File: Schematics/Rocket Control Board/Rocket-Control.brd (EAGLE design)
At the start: 21.9 x 35.5 mm, 23 parts

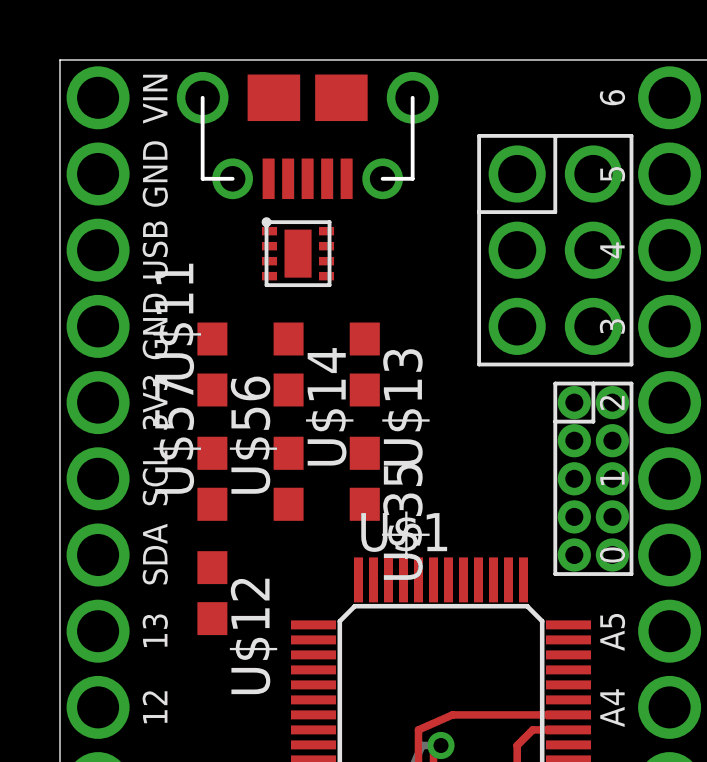
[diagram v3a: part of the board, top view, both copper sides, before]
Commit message: Added Diode, Began Routing
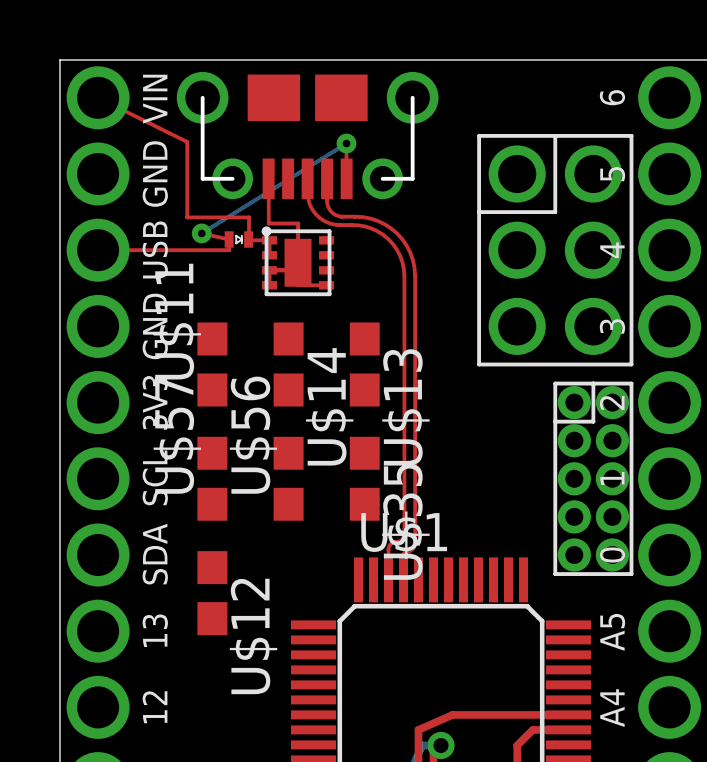
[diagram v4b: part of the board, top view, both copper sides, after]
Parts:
- added U$15: REGULATION-DIODE, RocketControlBoard:SOD-882
- moved U$5 0.30 mm to (6.99, 29.5)
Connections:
- net USB: now also U$15.P$1
- net VIN: now also U$15.P$2
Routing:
- net USB-P: track 0.00 -> 15.2 mm
- net USB-N: track 0.00 -> 15.0 mm
- net USB: track 0.00 -> 12.5 mm, vias 0 -> 2
- net VIN: track 0.00 -> 9.84 mm
- net GND: track 28.7 -> 37.2 mm
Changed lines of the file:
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@@
 <?xml version="1.0" encoding="utf-8"?>
 <!DOCTYPE eagle SYSTEM "eagle.dtd">
-<eagle version="7.5.0">
+<eagle version="7.6.0">
 <drawing>
 <settings>
@@
 <element name="U$21" library="RocketControlBoard" package="HEADER-SIDE-A" value="HEADER-SIDE-A" x="20.32" y="16.51"/>
 <element name="U$22" library="RocketControlBoard" package="HEADER-SIDE-B" value="HEADER-SIDE-B" x="1.27" y="36.83" rot="R90"/>
-<element name="U$5" library="RocketControlBoard" package="8-WFDFN-EXPOSED-PAD" value="REGULATOR" x="6.985" y="29.845" rot="R270"/>
+<element name="U$5" library="RocketControlBoard" package="8-WFDFN-EXPOSED-PAD" value="REGULATOR" x="6.985" y="29.5402" rot="R270"/>
 <element name="U$11" library="RocketControlBoard" package="C0603" value="REGULATOR-CAPACITORS" x="5.08" y="25.4" rot="R90"/>
 <element name="U$12" library="RocketControlBoard" package="C0603" value="REGULATOR-CAPACITORS" x="5.08" y="17.78" rot="R270"/>
 <element name="U$13" library="RocketControlBoard" package="C0603" value="REGULATOR-INDUCTOR" x="10.16" y="25.4" rot="R270"/>
 <element name="U$14" library="RocketControlBoard" package="C0603" value="REGULATOR-RESISTOR" x="7.62" y="25.4" rot="R270"/>
+<element name="U$15" library="RocketControlBoard" package="SOD-882" value="REGULATION-DIODE" x="5.6388" y="29.5656"/>
 </elements>
 <signals>
@@
 <contactref element="U$12" pad="1"/>
 <contactref element="U$5" pad="EXPOSED-THERMAL-PAD"/>
-<wire x1="8.885" y1="28.345" x2="7.935" y2="29.095" width="0" layer="19" extent="1-1"/>
-<wire x1="17.145" y1="19.05" x2="8.885" y2="28.345" width="0" layer="19" extent="1-1"/>
-<wire x1="10.16" y1="22.44" x2="17.145" y2="19.05" width="0" layer="19" extent="1-1"/>
-<wire x1="17.145" y1="21.59" x2="17.145" y2="19.05" width="0" layer="19" extent="1-1"/>
-<wire x1="17.145" y1="22.86" x2="17.145" y2="21.59" width="0" layer="19" extent="1-1"/>
-<wire x1="7.62" y1="22.44" x2="17.145" y2="21.59" width="0" layer="19" extent="1-1"/>
+<wire x1="6.985" y1="28.5402" x2="6.985" y2="28.0402" width="0.127" layer="1"/>
+<wire x1="8.885" y1="28.0402" x2="7.935" y2="28.0402" width="0.127" layer="1"/>
+<wire x1="7.935" y1="28.0402" x2="7.935" y2="28.7902" width="0.127" layer="1"/>
+<wire x1="6.985" y1="28.5402" x2="7.935" y2="28.5402" width="0.127" layer="1"/>
+<wire x1="7.935" y1="28.5402" x2="7.935" y2="28.7902" width="0.127" layer="1"/>
+<wire x1="6.955" y1="31.59" x2="6.9596" y2="31.59" width="0.127" layer="1"/>
+<wire x1="6.9596" y1="31.59" x2="6.9596" y2="30.099" width="0.127" layer="1"/>
+<wire x1="6.985" y1="28.5402" x2="7.9756" y2="28.5402" width="0.127" layer="1"/>
+<wire x1="7.9756" y1="28.5402" x2="7.9756" y2="28.829" width="0.127" layer="1"/>
+<wire x1="6.9596" y1="30.099" x2="7.935" y2="30.099" width="0.127" layer="1"/>
+<wire x1="7.935" y1="30.099" x2="7.935" y2="28.7902" width="0.127" layer="1"/>
+<wire x1="17.145" y1="22.86" x2="17.78" y2="26.67" width="0" layer="19" extent="1-1"/>
+<wire x1="17.145" y1="21.59" x2="17.145" y2="22.86" width="0" layer="19" extent="1-1"/>
+<wire x1="17.145" y1="19.05" x2="17.145" y2="21.59" width="0" layer="19" extent="1-1"/>
+<wire x1="16.95" y1="13.72" x2="17.145" y2="19.05" width="0" layer="19" extent="1-1"/>
+<wire x1="8.45" y1="14.22" x2="11.95" y2="13.22" width="0" layer="19" extent="1-1"/>
+<wire x1="10.45" y1="18.22" x2="8.45" y2="14.22" width="0" layer="19" extent="1-1"/>
+<wire x1="10.16" y1="22.44" x2="10.45" y2="18.22" width="0" layer="19" extent="1-1"/>
+<wire x1="7.62" y1="22.44" x2="10.16" y2="22.44" width="0" layer="19" extent="1-1"/>
 <wire x1="5.08" y1="22.44" x2="7.62" y2="22.44" width="0" layer="19" extent="1-1"/>
-<wire x1="10.45" y1="18.22" x2="5.08" y2="22.44" width="0" layer="19" extent="1-1"/>
-<wire x1="8.45" y1="14.22" x2="10.45" y2="18.22" width="0" layer="19" extent="1-1"/>
-<wire x1="11.95" y1="13.22" x2="8.45" y2="14.22" width="0" layer="19" extent="1-1"/>
-<wire x1="6.955" y1="31.59" x2="6.985" y2="28.845" width="0" layer="19" extent="1-1"/>
-<wire x1="17.78" y1="26.67" x2="6.955" y2="31.59" width="0" layer="19" extent="1-1"/>
-<wire x1="1.27" y1="26.67" x2="17.78" y2="26.67" width="0" layer="19" extent="1-1"/>
+<wire x1="5.08" y1="24.55" x2="5.08" y2="22.44" width="0" layer="19" extent="1-1"/>
+<wire x1="5.08" y1="18.63" x2="5.08" y2="22.44" width="0" layer="19" extent="1-1"/>
+<wire x1="6.985" y1="28.0402" x2="5.08" y2="24.55" width="0" layer="19" extent="1-1"/>
+<wire x1="1.27" y1="26.67" x2="5.08" y2="24.55" width="0" layer="19" extent="1-1"/>
 <wire x1="1.27" y1="31.75" x2="1.27" y2="26.67" width="0" layer="19" extent="1-1"/>
-<wire x1="5.08" y1="24.55" x2="8.89" y2="3.39" width="0" layer="19" extent="1-1"/>
-<wire x1="5.08" y1="18.63" x2="5.08" y2="24.55" width="0" layer="19" extent="1-1"/>
-<wire x1="7.935" y1="29.095" x2="6.985" y2="28.845" width="0" layer="19" extent="1-1"/>
-<wire x1="6.985" y1="28.845" x2="6.985" y2="28.345" width="0" layer="19" extent="1-1"/>
 </signal>
 <signal name="A0">
@@
 <contactref element="U$1" pad="33"/>
 <contactref element="U$38" pad="2:D-"/>
-<wire x1="11.45" y1="18.22" x2="8.905" y2="31.59" width="0" layer="19" extent="1-1"/>
+<wire x1="8.905" y1="31.59" x2="8.905" y2="30.8714" width="0.127" layer="1"/>
+<wire x1="8.905" y1="30.8714" x2="9.398" y2="30.3276" width="0.127" layer="1" curve="90"/>
+<wire x1="9.398" y1="30.3276" x2="9.8298" y2="30.3276" width="0.127" layer="1"/>
+<wire x1="9.8298" y1="30.3276" x2="11.8364" y2="28.3718" width="0.127" layer="1" curve="-90"/>
+<wire x1="11.8364" y1="28.3718" x2="11.8364" y2="19.4564" width="0.127" layer="1"/>
+<wire x1="11.8364" y1="19.4564" x2="11.5316" y2="19.1516" width="0.127" layer="1" curve="-90"/>
+<wire x1="11.5316" y1="19.1516" x2="11.45" y2="19.0192" width="0.127" layer="1" curve="90"/>
+<wire x1="11.45" y1="19.0192" x2="11.45" y2="18.22" width="0.127" layer="1"/>
 </signal>
 <signal name="USB-P">
 <contactref element="U$1" pad="34"/>
 <contactref element="U$38" pad="3:D+"/>
-<wire x1="10.95" y1="18.22" x2="8.255" y2="31.59" width="0" layer="19" extent="1-1"/>
+<wire x1="8.255" y1="31.59" x2="8.255" y2="31.1658" width="0.127" layer="1"/>
+<wire x1="8.255" y1="31.1658" x2="9.2964" y2="30.0482" width="0.127" layer="1" curve="90"/>
+<wire x1="9.2964" y1="30.0482" x2="9.7282" y2="30.0482" width="0.127" layer="1"/>
+<wire x1="9.7282" y1="30.0482" x2="11.4808" y2="28.3718" width="0.127" layer="1" curve="-90"/>
+<wire x1="11.4808" y1="28.3718" x2="11.4808" y2="19.7612" width="0.127" layer="1"/>
+<wire x1="11.4808" y1="19.7612" x2="11.2014" y2="19.4818" width="0.127" layer="1" curve="-90"/>
+<wire x1="11.2014" y1="19.4818" x2="10.95" y2="19.2304" width="0.127" layer="1" curve="90"/>
+<wire x1="10.95" y1="19.2304" x2="10.95" y2="18.22" width="0.127" layer="1"/>
 </signal>
 <signal name="VDDIO-B">
@@
 <contactref element="U$38" pad="1:VBUS"/>
 <contactref element="U$22" pad="USB"/>
-<wire x1="1.27" y1="29.21" x2="9.555" y2="31.59" width="0" layer="19" extent="1-1"/>
+<contactref element="U$15" pad="P$1"/>
+<wire x1="5.6388" y1="29.5656" x2="5.6388" y2="29.21" width="0.127" layer="1"/>
+<wire x1="5.6388" y1="29.21" x2="1.27" y2="29.21" width="0.127" layer="1"/>
+<wire x1="9.555" y1="31.59" x2="9.5504" y2="31.59" width="0.127" layer="1"/>
+<wire x1="9.5504" y1="31.59" x2="9.5504" y2="32.766" width="0.127" layer="1"/>
+<via x="9.5504" y="32.766" extent="1-16" drill="0.254"/>
+<wire x1="9.5504" y1="32.766" x2="4.7244" y2="29.7688" width="0.127" layer="16"/>
+<via x="4.7244" y="29.7688" extent="1-16" drill="0.254"/>
+<wire x1="4.7244" y1="29.7688" x2="5.6388" y2="29.5656" width="0.127" layer="1"/>
 </signal>
 <signal name="RX">
@@
 <contactref element="U$11" pad="2"/>
 <contactref element="U$5" pad="VIN"/>
-<wire x1="1.27" y1="34.29" x2="6.985" y2="29.845" width="0" layer="19" extent="1-1"/>
-<wire x1="5.08" y1="26.25" x2="6.985" y2="29.345" width="0" layer="19" extent="1-1"/>
-<wire x1="6.985" y1="29.345" x2="6.985" y2="29.845" width="0" layer="19" extent="1-1"/>
+<contactref element="U$15" pad="P$2"/>
+<wire x1="6.985" y1="29.5402" x2="6.3142" y2="29.5402" width="0.127" layer="1"/>
+<wire x1="6.3142" y1="29.5402" x2="6.2888" y2="29.5656" width="0.127" layer="1"/>
+<wire x1="5.08" y1="26.25" x2="6.985" y2="29.0402" width="0" layer="19" extent="1-1"/>
+<wire x1="6.985" y1="29.5402" x2="6.985" y2="29.0402" width="0.127" layer="1"/>
+<wire x1="6.2888" y1="29.5656" x2="6.2992" y2="29.5656" width="0.127" layer="1"/>
+<wire x1="6.2992" y1="29.5656" x2="6.2992" y2="30.3022" width="0.127" layer="1"/>
+<wire x1="6.2992" y1="30.3022" x2="4.2418" y2="30.3022" width="0.127" layer="1"/>
+<wire x1="4.2418" y1="30.3022" x2="4.2418" y2="32.8168" width="0.127" layer="1"/>
+<wire x1="4.2418" y1="32.8168" x2="1.27" y2="34.29" width="0.127" layer="1"/>
 </signal>
 <signal name="A5">
@@
 <contactref element="U$12" pad="2"/>
 <contactref element="U$5" pad="SW"/>
-<wire x1="5.08" y1="20.74" x2="8.885" y2="29.345" width="0" layer="19" extent="1-1"/>
+<wire x1="5.08" y1="20.74" x2="8.885" y2="29.0402" width="0" layer="19" extent="1-1"/>
 <wire x1="8.45" y1="13.22" x2="5.08" y2="20.74" width="0" layer="19" extent="1-1"/>
 <wire x1="5.08" y1="16.93" x2="8.45" y2="13.22" width="0" layer="19" extent="1-1"/>
@@
 <contactref element="U$5" pad="PG"/>
 <contactref element="U$13" pad="1"/>
-<wire x1="10.16" y1="26.25" x2="8.885" y2="29.845" width="0" layer="19" extent="1-1"/>
+<wire x1="10.16" y1="26.25" x2="8.885" y2="29.5402" width="0" layer="19" extent="1-1"/>
 </signal>
 <signal name="N$3">
 <contactref element="U$14" pad="1"/>
 <contactref element="U$5" pad="VOS"/>
-<wire x1="7.62" y1="26.25" x2="8.885" y2="28.845" width="0" layer="19" extent="1-1"/>
+<wire x1="7.62" y1="26.25" x2="8.885" y2="28.5402" width="0" layer="19" extent="1-1"/>
 </signal>
 </signals>

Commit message: Misc Routing
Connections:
- net +3V3: now also U$12.2, U$13.2, U$14.2, U$5.SW
- net VIN-REGULATED: no longer U$12.2, U$13.2, U$14.2, U$5.SW
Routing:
- net +3V3: track 0.00 -> 41.6 mm, vias 0 -> 1
- net GND: track 37.2 -> 55.8 mm, vias 0 -> 1
- net SDA: track 0.00 -> 15.0 mm, vias 0 -> 1
- net SCL: track 0.00 -> 14.9 mm, vias 0 -> 1
- net N$1: track 0.00 -> 4.60 mm
- net VIN: track 9.84 -> 13.8 mm
- net N$3: track 0.00 -> 3.92 mm
